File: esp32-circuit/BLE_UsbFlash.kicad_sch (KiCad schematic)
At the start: 0 parts

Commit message: the 0G
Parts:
- added C1: C, symbol Device:C
- added D1: LED, symbol Device:LED
- added J1: USB_A, Connector_USB:USB_A_Connfly_DS1098_Horizontal, symbol Connector:USB_A
- added J2: Micro_SD_Card, symbol Connector:Micro_SD_Card
- added R1, R2: R, symbol Device:R
- added SW1: SW_Push, symbol Switch:SW_Push
- added U1: ESP32-S3-WROOM-1, RF_Module:ESP32-S3-WROOM-1, symbol RF_Module:ESP32-S3-WROOM-1
- added U3: AMS1117-3.3, Package_TO_SOT_SMD:SOT-223-3_TabPin2, symbol Regulator_Linear:AMS1117-3.3
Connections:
- new net: SW1.2, U1.17 (IO9)
- new net: D1.2 (A), U1.15 (IO3)
- new net: J1.2 (D-), R1.2
- new net: J1.3 (D+), R2.2
- new net 3.3V: J2.4 (VDD), U1.2 (3V3), U3.2 (VO)
- new net 5V: J1.1 (VBUS), U3.3 (VI)
- new net CLK: J2.5 (CLK), U1.29 (IO36)
- new net CMD: J2.3 (CMD), U1.28 (IO35)
- new net D+: R2.1, U1.14 (USB_D+)
- new net D-: R1.1, U1.13 (USB_D-)
- new net DAT0: J2.7 (DAT0), U1.30 (IO37)
- new net DAT1: J2.8 (DAT1), U1.31 (IO38)
- new net DAT2: J2.1 (DAT2), U1.32 (IO39)
- new net DAT3: J2.2 (DAT3/CD), U1.33 (IO40)
- new net GND: D1.1 (K), J1.4 (GND), J1.5 (Shield), J2.6 (VSS), SW1.1, U1.1 (GND), U1.40 (GND), U1.41 (GND), U3.1 (GND)

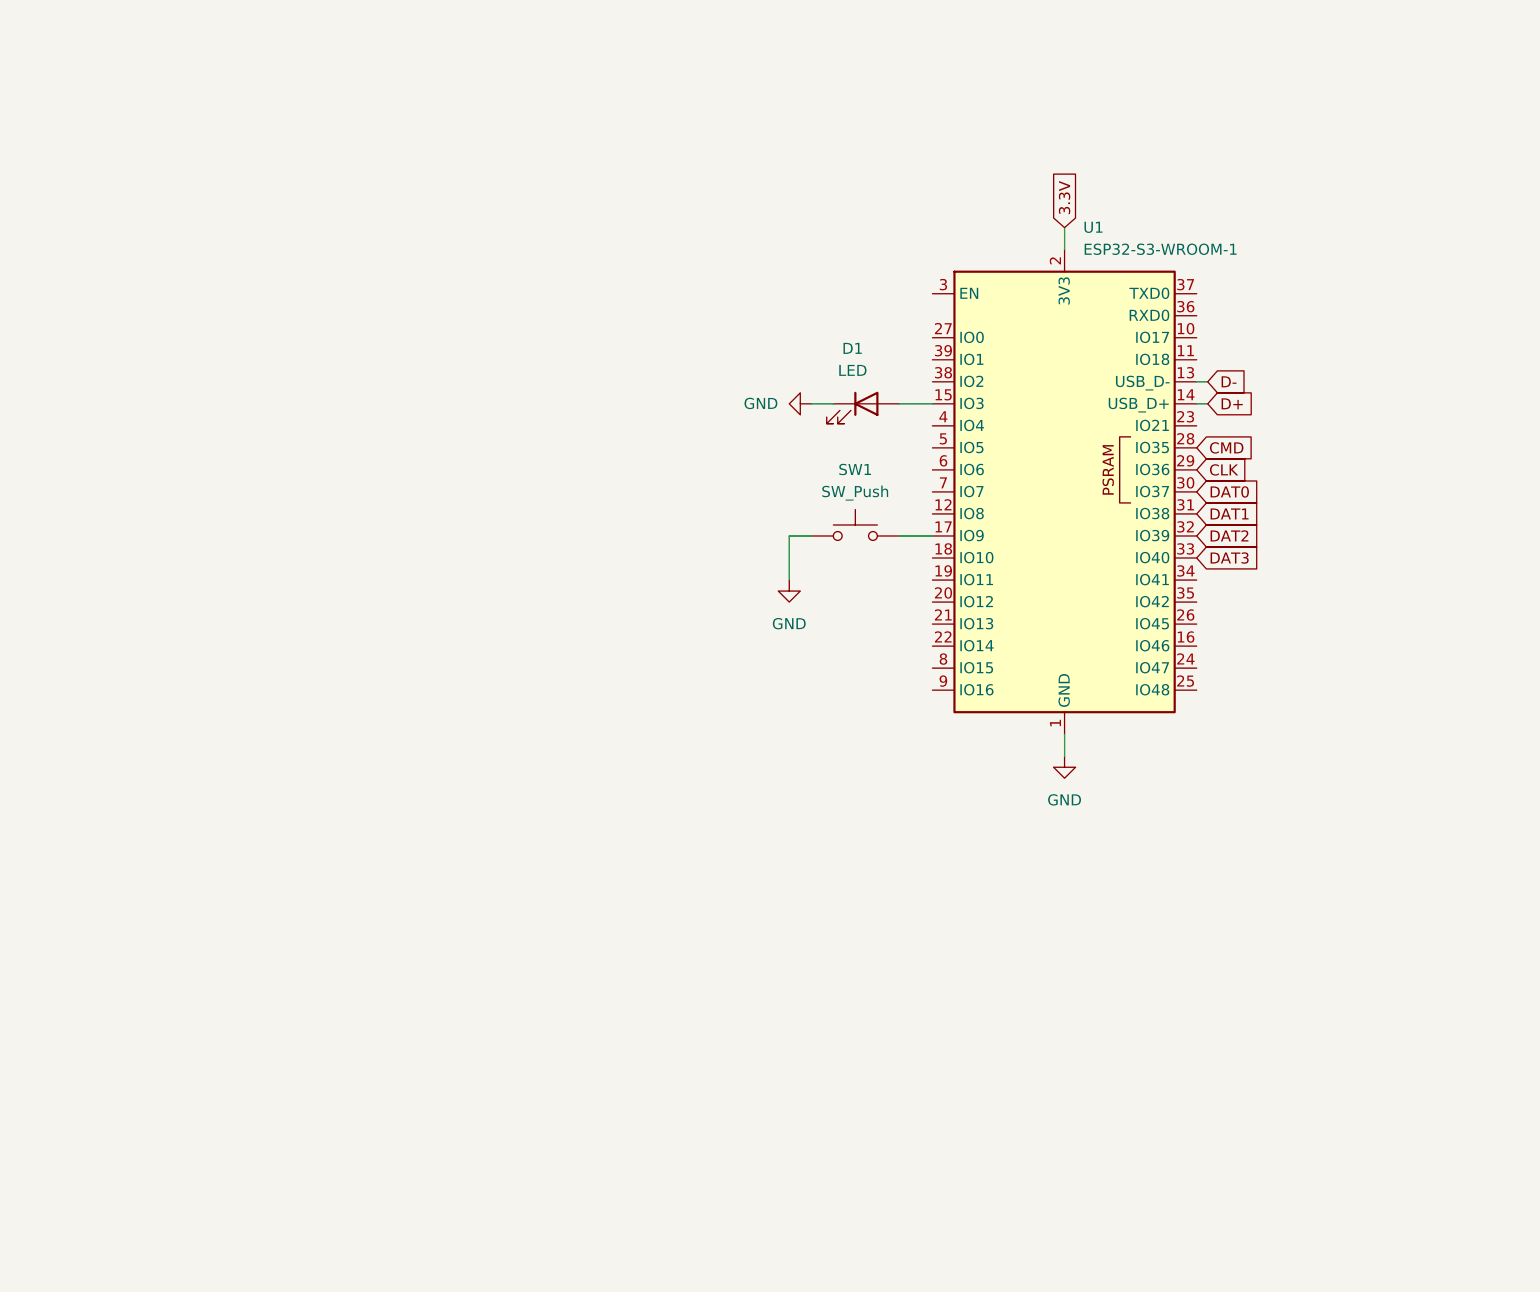
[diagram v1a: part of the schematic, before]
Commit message: Update BLE_UsbFlash.kicad_sch
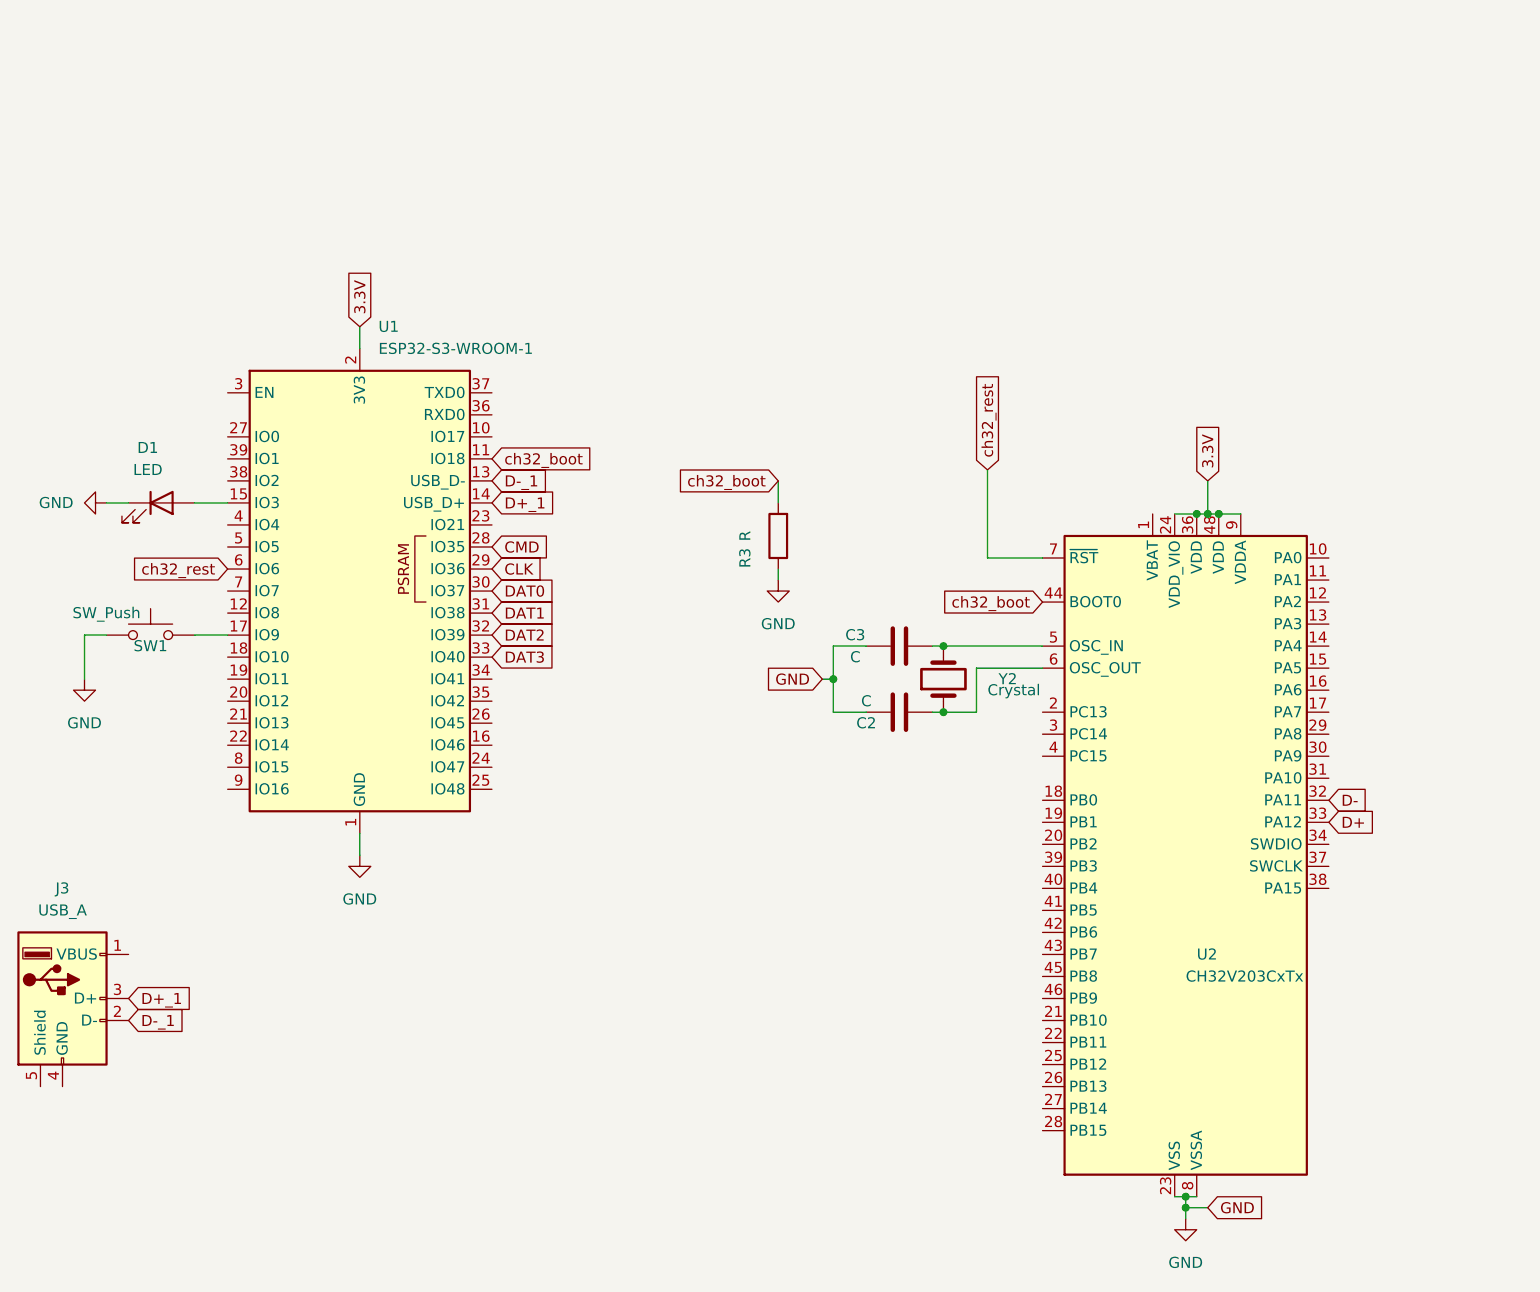
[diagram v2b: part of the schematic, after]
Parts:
- added C2, C3: C, symbol Device:C
- added J3: USB_A, symbol Connector:USB_A
- added R3: R, symbol Device:R
- added U2: CH32V203CxTx, Package_QFP:LQFP-48_7x7mm_P0.5mm, symbol MCU_WCH_RiscV:CH32V203CxTx
- added Y2: Crystal, symbol Device:Crystal
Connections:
- net 3.3V: now also U2.24 (VDD_VIO), U2.36 (VDD), U2.48 (VDD), U2.9 (VDDA)
- net D+: now also U2.33 (PA12); no longer U1.14 (USB_D+)
- net D-: now also U2.32 (PA11); no longer U1.13 (USB_D-)
- net GND: now also C2.2, C3.2, R3.1, U2.23 (VSS), U2.35 (VSS), U2.47 (VSS), U2.8 (VSSA)
- net ch32_boot: now reaches U1.11 (IO18)
- net ch32_boot: now also R3.2, U2.44 (BOOT0)
- net ch32_rest: now reaches U1.6 (IO6)
- net ch32_rest: now also U2.7 (~{RST})
- new net: C3.1, U2.5 (OSC_IN), Y2.2
- new net: C2.1, U2.6 (OSC_OUT), Y2.1
- new net D+_1: J3.3 (D+), U1.14 (USB_D+)
- new net D-_1: J3.2 (D-), U1.13 (USB_D-)
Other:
- moved on the sheet: D1, SW1, U1

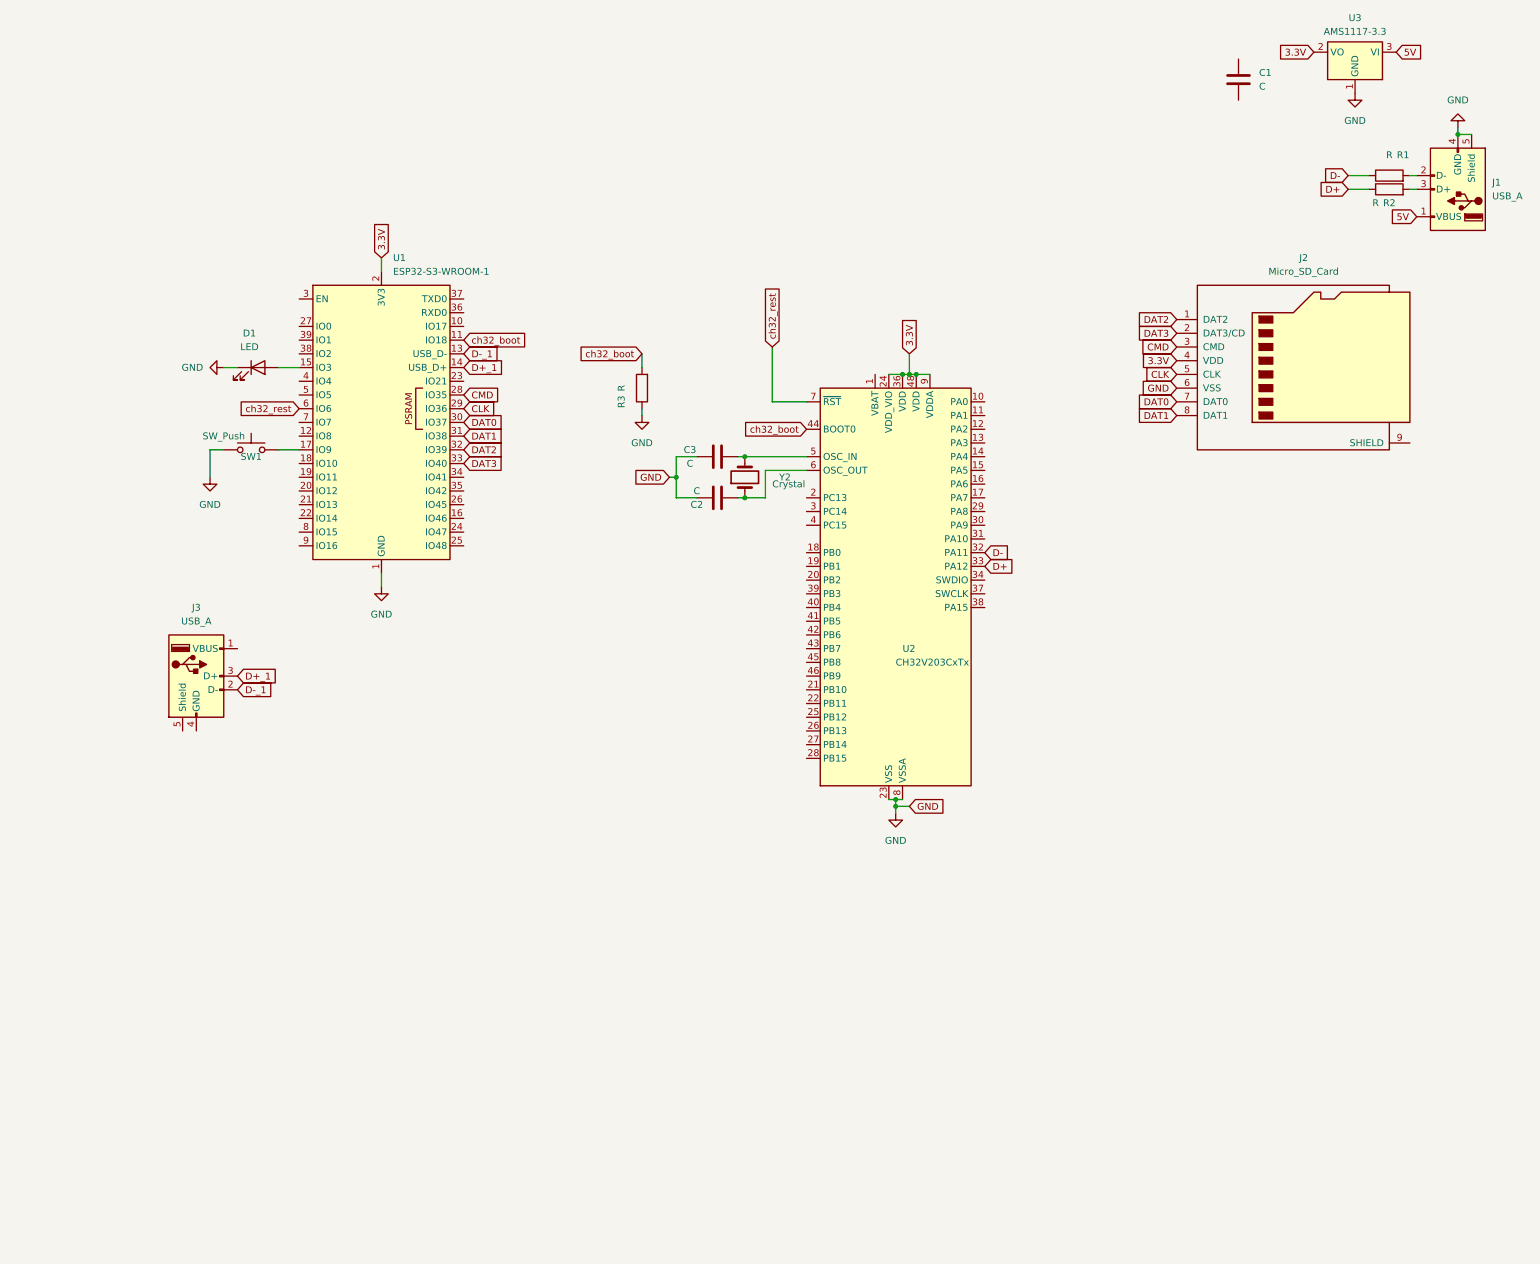
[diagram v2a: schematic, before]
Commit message: sepret_usb
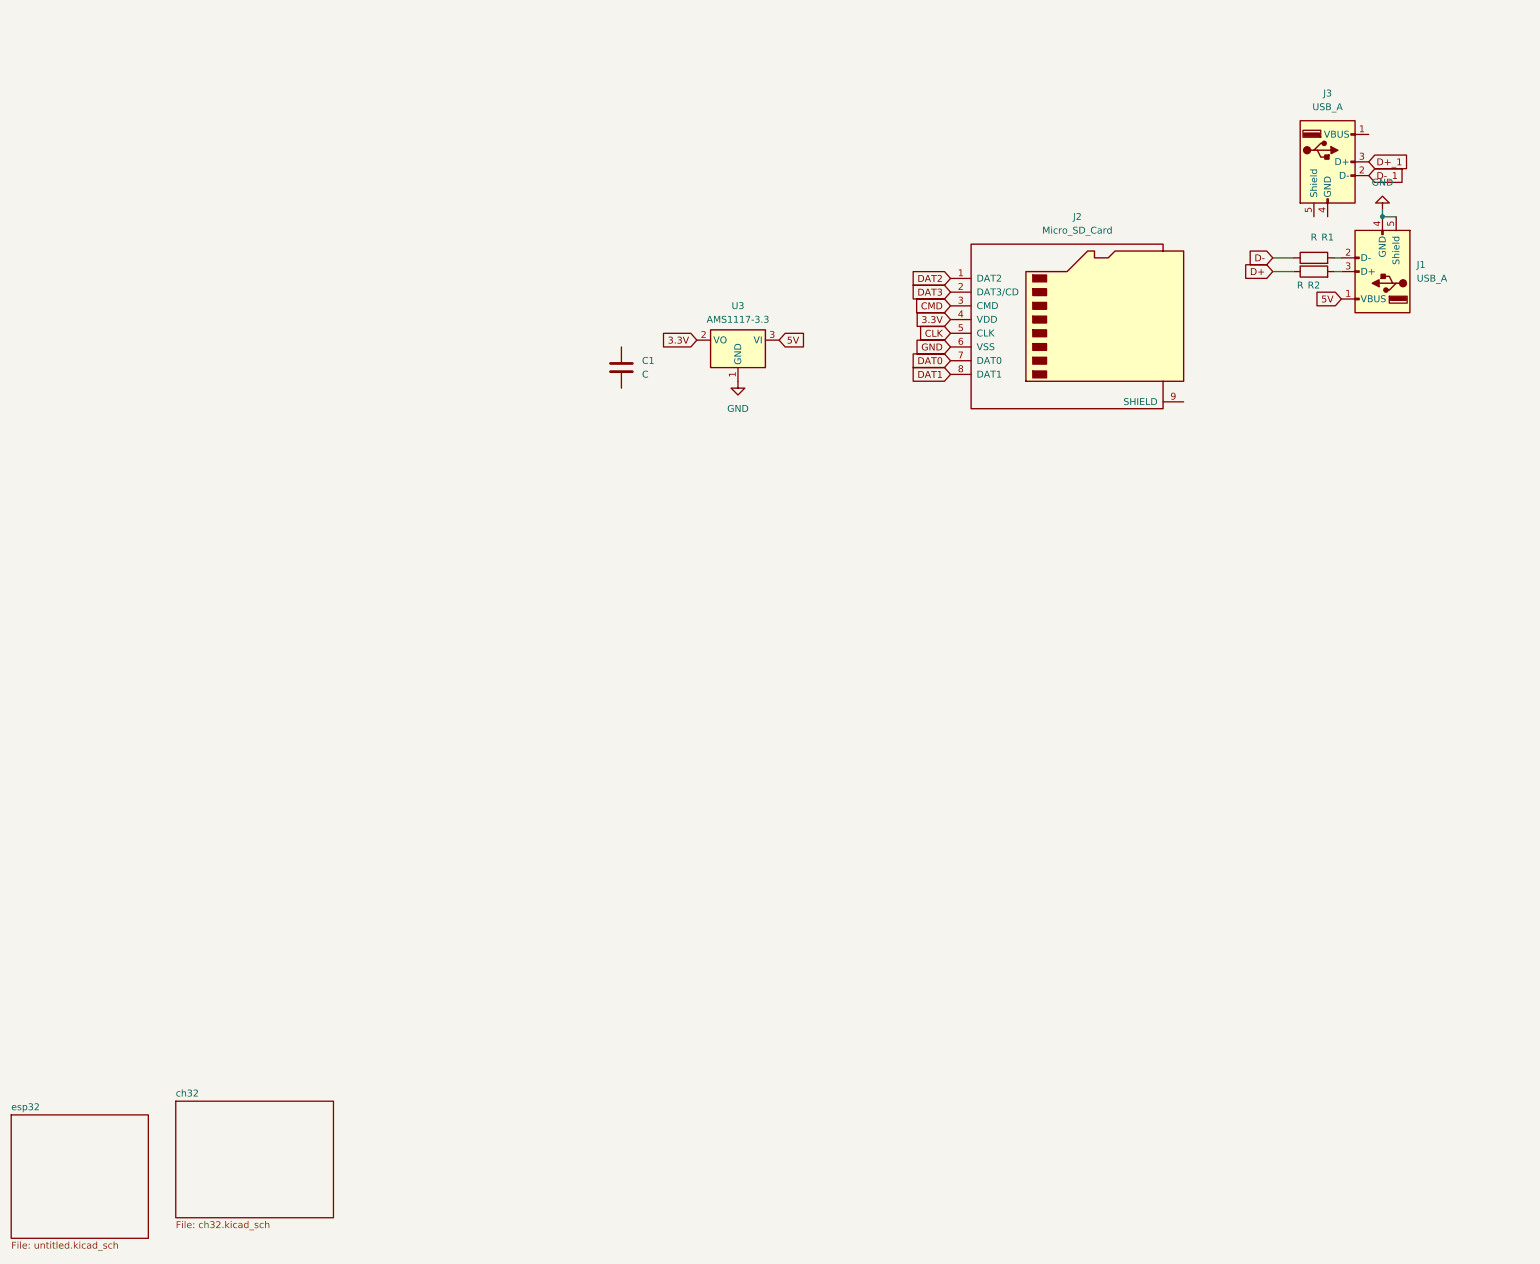
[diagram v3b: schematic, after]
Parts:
- removed C2, C3: C, symbol Device:C
- removed D1: LED, symbol Device:LED
- removed R3: R, symbol Device:R
- removed SW1: SW_Push, symbol Switch:SW_Push
- removed U1: ESP32-S3-WROOM-1, RF_Module:ESP32-S3-WROOM-1, symbol RF_Module:ESP32-S3-WROOM-1
- removed U2: CH32V203CxTx, Package_QFP:LQFP-48_7x7mm_P0.5mm, symbol MCU_WCH_RiscV:CH32V203CxTx
- removed Y2: Crystal, symbol Device:Crystal
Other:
- added sheet ch32 (ch32.kicad_sch)
- added sheet esp32 (untitled.kicad_sch)
- moved on the sheet: C1, J1, J2, J3, R1, R2, U3
